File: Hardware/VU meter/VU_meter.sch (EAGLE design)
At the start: 21 parts, among them IC1 ATMEGA328-PU, IC2 NE5532N, Q1 16M

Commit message: firmware and hardware update
Put a capacitor at the amplifier output, incorporated neopixel strip to
show audio level
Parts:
- added C6, C9: 100p, capacitor-wima:C5/5
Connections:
- new net N$13: C10.2, C6.1, IC2B.OUT, R7.1
- new net N$7: C6.2, IC1.ANALOG_0
- net N$12: now also C9.2; no longer C4.2, IC2A.OUT, R9.1
- net N$9: now also C4.2, C9.1, IC2A.OUT, R9.1; no longer C10.2, IC1.ANALOG_0, IC2B.OUT, R7.1
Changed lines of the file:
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@@
 <part name="C4" library="capacitor-wima" deviceset="C" device="5/5" value="47p"/>
 <part name="C10" library="capacitor-wima" deviceset="C" device="5/5" value="47p"/>
+<part name="C6" library="capacitor-wima" deviceset="C" device="5/5" value="100p"/>
+<part name="C9" library="capacitor-wima" deviceset="C" device="5/5" value="100p"/>
 </parts>
 <sheets>
@@
 <instance part="C4" gate="G$1" x="60.96" y="205.74" rot="R90"/>
 <instance part="C10" gate="G$1" x="60.96" y="149.86" rot="R90"/>
+<instance part="C6" gate="G$1" x="78.74" y="129.54" rot="R90"/>
+<instance part="C9" gate="G$1" x="86.36" y="185.42" rot="R90"/>
 </instances>
 <busses>
@@
 </segment>
 </net>
-<net name="N$9" class="0">
-<segment>
-<wire x1="66.04" y1="149.86" x2="68.58" y2="149.86" width="0.1524" layer="91"/>
-<wire x1="68.58" y1="149.86" x2="68.58" y2="144.78" width="0.1524" layer="91"/>
-<pinref part="R7" gate="G$1" pin="1"/>
-<wire x1="68.58" y1="144.78" x2="68.58" y2="139.7" width="0.1524" layer="91"/>
-<wire x1="68.58" y1="139.7" x2="66.04" y2="139.7" width="0.1524" layer="91"/>
-<junction x="68.58" y="144.78"/>
-<pinref part="IC2" gate="B" pin="OUT"/>
-<wire x1="58.42" y1="129.54" x2="73.66" y2="129.54" width="0.1524" layer="91"/>
-<wire x1="73.66" y1="129.54" x2="73.66" y2="144.78" width="0.1524" layer="91"/>
-<wire x1="73.66" y1="144.78" x2="68.58" y2="144.78" width="0.1524" layer="91"/>
-<junction x="73.66" y="129.54"/>
-<pinref part="IC1" gate="1" pin="ANALOG_0"/>
-<wire x1="43.18" y1="83.82" x2="73.66" y2="83.82" width="0.1524" layer="91"/>
-<wire x1="73.66" y1="83.82" x2="73.66" y2="129.54" width="0.1524" layer="91"/>
-<pinref part="C10" gate="G$1" pin="2"/>
-</segment>
-</net>
 <net name="LEFT" class="0">
 <segment>
@@
 <net name="N$12" class="0">
 <segment>
+<pinref part="IC1" gate="1" pin="ANALOG_1"/>
+<wire x1="43.18" y1="81.28" x2="106.68" y2="81.28" width="0.1524" layer="91"/>
+<wire x1="106.68" y1="81.28" x2="106.68" y2="185.42" width="0.1524" layer="91"/>
+<pinref part="C9" gate="G$1" pin="2"/>
+<wire x1="91.44" y1="185.42" x2="106.68" y2="185.42" width="0.1524" layer="91"/>
+</segment>
+</net>
+<net name="N$7" class="0">
+<segment>
+<pinref part="IC1" gate="1" pin="ANALOG_0"/>
+<wire x1="43.18" y1="83.82" x2="88.9" y2="83.82" width="0.1524" layer="91"/>
+<wire x1="88.9" y1="83.82" x2="88.9" y2="129.54" width="0.1524" layer="91"/>
+<pinref part="C6" gate="G$1" pin="2"/>
+<wire x1="83.82" y1="129.54" x2="88.9" y2="129.54" width="0.1524" layer="91"/>
+</segment>
+</net>
+<net name="N$9" class="0">
+<segment>
+<pinref part="R9" gate="G$1" pin="1"/>
+<wire x1="68.58" y1="195.58" x2="66.04" y2="195.58" width="0.1524" layer="91"/>
+<pinref part="C4" gate="G$1" pin="2"/>
 <wire x1="66.04" y1="205.74" x2="68.58" y2="205.74" width="0.1524" layer="91"/>
 <wire x1="68.58" y1="205.74" x2="68.58" y2="200.66" width="0.1524" layer="91"/>
-<pinref part="R9" gate="G$1" pin="1"/>
 <wire x1="68.58" y1="200.66" x2="68.58" y2="195.58" width="0.1524" layer="91"/>
-<wire x1="68.58" y1="195.58" x2="66.04" y2="195.58" width="0.1524" layer="91"/>
 <junction x="68.58" y="200.66"/>
+<wire x1="73.66" y1="200.66" x2="68.58" y2="200.66" width="0.1524" layer="91"/>
+<pinref part="IC2" gate="A" pin="OUT"/>
 <wire x1="60.96" y1="185.42" x2="73.66" y2="185.42" width="0.1524" layer="91"/>
 <wire x1="73.66" y1="185.42" x2="73.66" y2="200.66" width="0.1524" layer="91"/>
-<wire x1="73.66" y1="200.66" x2="68.58" y2="200.66" width="0.1524" layer="91"/>
-<pinref part="IC2" gate="A" pin="OUT"/>
 <junction x="73.66" y="185.42"/>
-<pinref part="IC1" gate="1" pin="ANALOG_1"/>
-<wire x1="43.18" y1="81.28" x2="81.28" y2="81.28" width="0.1524" layer="91"/>
-<wire x1="81.28" y1="81.28" x2="81.28" y2="185.42" width="0.1524" layer="91"/>
-<wire x1="81.28" y1="185.42" x2="73.66" y2="185.42" width="0.1524" layer="91"/>
-<pinref part="C4" gate="G$1" pin="2"/>
-</segment>
-</net>
+<pinref part="C9" gate="G$1" pin="1"/>
+<wire x1="83.82" y1="185.42" x2="73.66" y2="185.42" width="0.1524" layer="91"/>
+</segment>
+</net>
+<net name="N$13" class="0">
+<segment>
+<pinref part="R7" gate="G$1" pin="1"/>
+<wire x1="68.58" y1="139.7" x2="66.04" y2="139.7" width="0.1524" layer="91"/>
+<pinref part="C10" gate="G$1" pin="2"/>
+<wire x1="66.04" y1="149.86" x2="68.58" y2="149.86" width="0.1524" layer="91"/>
+<wire x1="68.58" y1="149.86" x2="68.58" y2="144.78" width="0.1524" layer="91"/>
+<junction x="68.58" y="144.78"/>
+<wire x1="68.58" y1="144.78" x2="68.58" y2="139.7" width="0.1524" layer="91"/>
+<wire x1="73.66" y1="144.78" x2="68.58" y2="144.78" width="0.1524" layer="91"/>
+<wire x1="73.66" y1="144.78" x2="73.66" y2="129.54" width="0.1524" layer="91"/>
+<pinref part="IC2" gate="B" pin="OUT"/>
+<wire x1="58.42" y1="129.54" x2="73.66" y2="129.54" width="0.1524" layer="91"/>
+<junction x="73.66" y="129.54"/>
+<pinref part="C6" gate="G$1" pin="1"/>
+<wire x1="76.2" y1="129.54" x2="73.66" y2="129.54" width="0.1524" layer="91"/>
+</segment>
+</net>

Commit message: Cycle colors mode, modes change
New buttont for modes change, new mode for cycling colors (now total 4
modes). Changed mode is written to EEPROM and read from EEPROM when
device boots up. Changes in code and schematics.
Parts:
- added C11: 0.1u, capacitor-wima:C5/5
- added R10: 10k, eagle-ltspice:R0207/10
- added S2: PVA1R, switch-misc:PVA1R
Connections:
- new net N$14: C11.2, IC1.DIGITAL_2, R10.2, S22.P
- net GND: now also C11.1, R10.1
- net VCC: now also S22.S
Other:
- note added: "Changes mode"
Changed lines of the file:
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@@
 <part name="C6" library="capacitor-wima" deviceset="C" device="5/5" value="100p"/>
 <part name="C9" library="capacitor-wima" deviceset="C" device="5/5" value="100p"/>
+<part name="S2" library="switch-misc" deviceset="PVA1R" device=""/>
+<part name="P+4" library="supply1" deviceset="VCC" device=""/>
+<part name="R10" library="eagle-ltspice" deviceset="R" device="0207/10" value="10k"/>
+<part name="GND7" library="supply1" deviceset="GND" device=""/>
+<part name="C11" library="capacitor-wima" deviceset="C" device="5/5" value="0.1u"/>
+<part name="GND8" library="supply1" deviceset="GND" device=""/>
 </parts>
 <sheets>
 <sheet>
 <plain>
+<text x="76.2" y="50.8" size="1.778" layer="91">Changes mode</text>
 </plain>
 <instances>
@@
 <instance part="C6" gate="G$1" x="78.74" y="129.54" rot="R90"/>
 <instance part="C9" gate="G$1" x="86.36" y="185.42" rot="R90"/>
+<instance part="S2" gate="1" x="78.74" y="60.96" rot="R270"/>
+<instance part="S2" gate="2" x="78.74" y="55.88" rot="R270"/>
+<instance part="P+4" gate="VCC" x="91.44" y="63.5"/>
+<instance part="R10" gate="G$1" x="71.12" y="50.8" rot="R90"/>
+<instance part="GND7" gate="1" x="71.12" y="43.18"/>
+<instance part="C11" gate="G$1" x="63.5" y="48.26" rot="R180"/>
+<instance part="GND8" gate="1" x="63.5" y="43.18"/>
 </instances>
 <busses>
@@
 <wire x1="25.4" y1="198.12" x2="25.4" y2="200.66" width="0.1524" layer="91"/>
 </segment>
+<segment>
+<pinref part="S2" gate="2" pin="S"/>
+<pinref part="P+4" gate="VCC" pin="VCC"/>
+<wire x1="83.82" y1="55.88" x2="91.44" y2="55.88" width="0.1524" layer="91"/>
+<wire x1="91.44" y1="55.88" x2="91.44" y2="60.96" width="0.1524" layer="91"/>
+</segment>
 </net>
 <net name="GND" class="0">
@@
 <wire x1="0" y1="116.84" x2="-10.16" y2="116.84" width="0.1524" layer="91"/>
 <label x="-10.16" y="116.84" size="1.778" layer="95" rot="R180" xref="yes"/>
+</segment>
+<segment>
+<pinref part="R10" gate="G$1" pin="1"/>
+<pinref part="GND7" gate="1" pin="GND"/>
+</segment>
+<segment>
+<pinref part="C11" gate="G$1" pin="1"/>
+<pinref part="GND8" gate="1" pin="GND"/>
 </segment>
 </net>
@@
 </segment>
 </net>
+<net name="N$14" class="0">
+<segment>
+<pinref part="IC1" gate="1" pin="DIGITAL_2"/>
+<pinref part="S2" gate="2" pin="P"/>
+<wire x1="43.18" y1="55.88" x2="63.5" y2="55.88" width="0.1524" layer="91"/>
+<pinref part="R10" gate="G$1" pin="2"/>
+<wire x1="63.5" y1="55.88" x2="71.12" y2="55.88" width="0.1524" layer="91"/>
+<wire x1="71.12" y1="55.88" x2="73.66" y2="55.88" width="0.1524" layer="91"/>
+<junction x="71.12" y="55.88"/>
+<pinref part="C11" gate="G$1" pin="2"/>
+<wire x1="63.5" y1="53.34" x2="63.5" y2="55.88" width="0.1524" layer="91"/>
+</segment>
+</net>

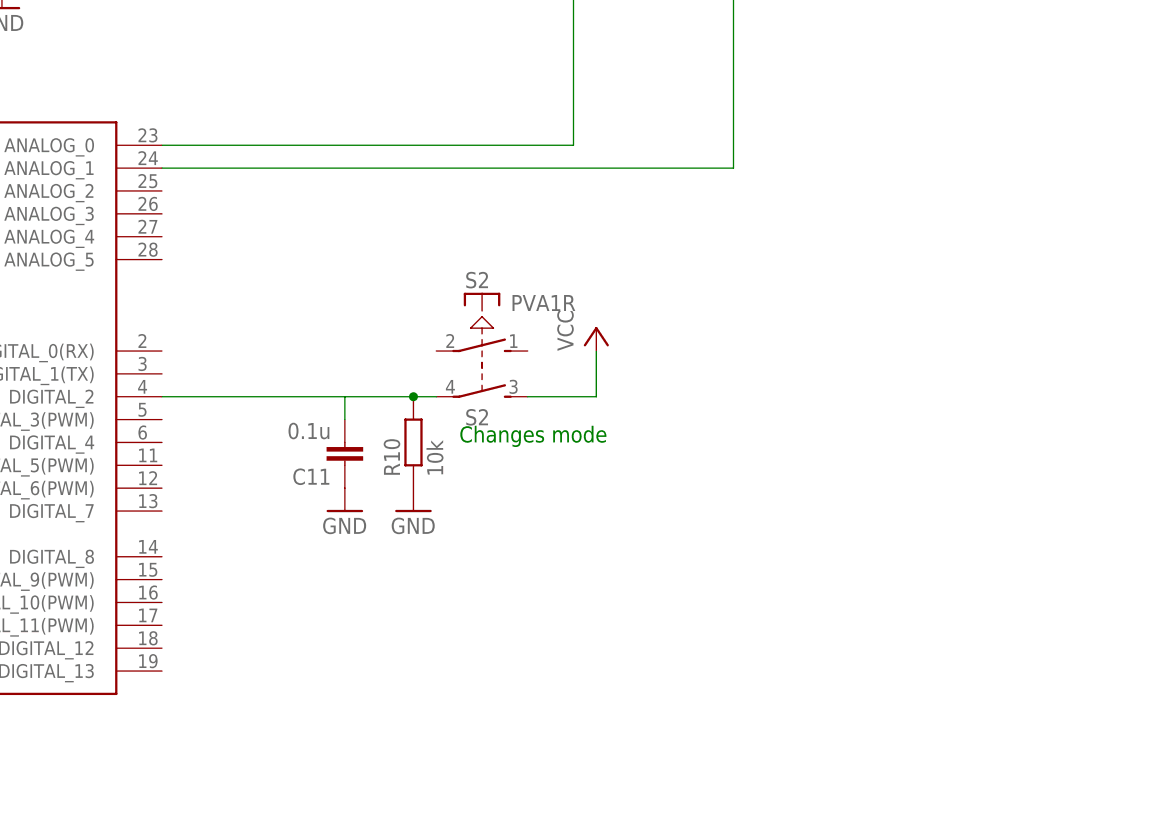
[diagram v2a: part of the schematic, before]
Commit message: potentiometer attached
Potentiometer enabling button and pot itself attached in schematics and
code.
Prototyping complete on breadboard
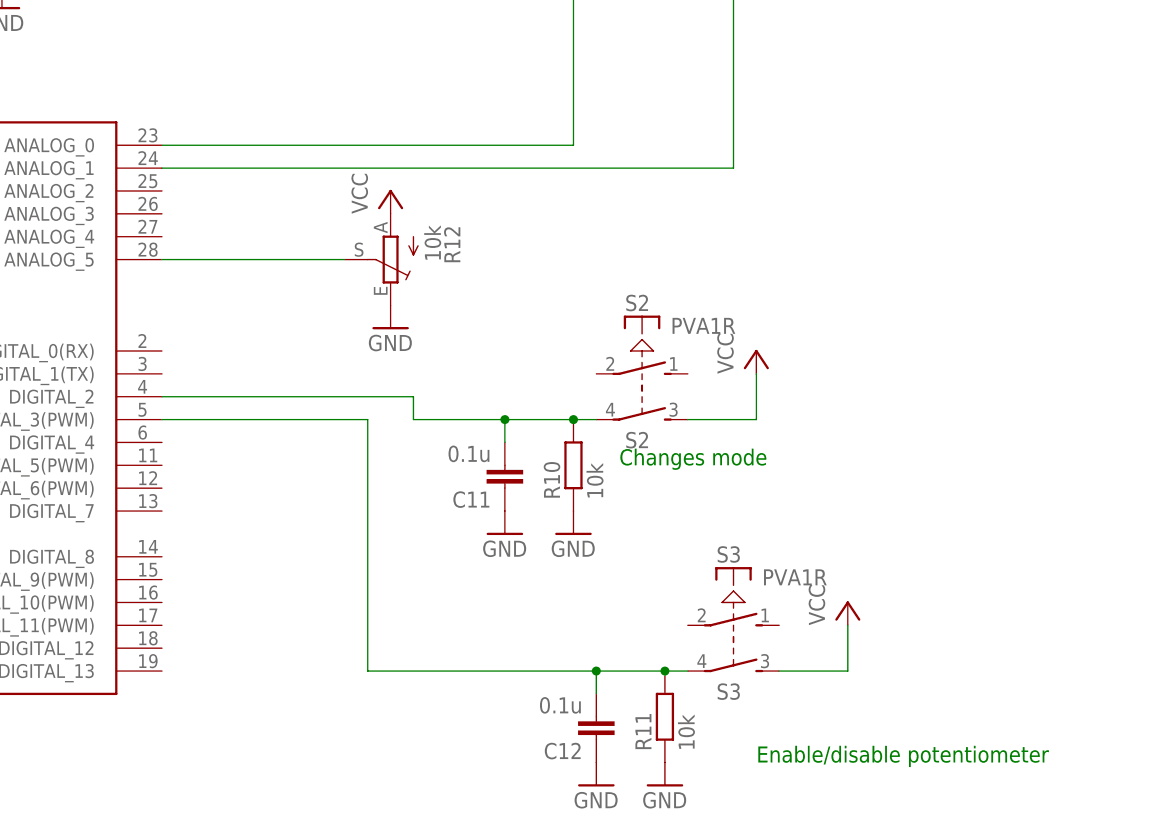
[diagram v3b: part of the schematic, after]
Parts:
- added C12: 0.1u, capacitor-wima:C5/5
- added R11: 10k, eagle-ltspice:R0207/10
- added R12: 10k, pot:TRIM_EU-CIP20C-6MM
- added S3: PVA1R, switch-misc:PVA1R
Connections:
- new net N$16: C12.2, IC1.DIGITAL_3(PWM), R11.2, S32.P
- new net N$17: IC1.ANALOG_5, R12.S
- net GND: now also C12.1, R11.1, R12.E
- net VCC: now also R12.A, S32.S
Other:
- note added: "Enable/disable potentiometer"
- moved on the sheet: C11, R10, S2
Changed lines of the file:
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@@
 <part name="C11" library="capacitor-wima" deviceset="C" device="5/5" value="0.1u"/>
 <part name="GND8" library="supply1" deviceset="GND" device=""/>
+<part name="S3" library="switch-misc" deviceset="PVA1R" device=""/>
+<part name="P+5" library="supply1" deviceset="VCC" device=""/>
+<part name="R11" library="eagle-ltspice" deviceset="R" device="0207/10" value="10k"/>
+<part name="GND9" library="supply1" deviceset="GND" device=""/>
+<part name="C12" library="capacitor-wima" deviceset="C" device="5/5" value="0.1u"/>
+<part name="GND10" library="supply1" deviceset="GND" device=""/>
+<part name="R12" library="pot" deviceset="TRIM_EU-" device="CIP20C-6MM" value="10k"/>
+<part name="P+6" library="supply1" deviceset="VCC" device=""/>
+<part name="GND11" library="supply1" deviceset="GND" device=""/>
 </parts>
 <sheets>
 <sheet>
 <plain>
-<text x="76.2" y="50.8" size="1.778" layer="91">Changes mode</text>
+<text x="93.98" y="48.26" size="1.778" layer="91">Changes mode</text>
+<text x="109.22" y="15.24" size="1.778" layer="91">Enable/disable potentiometer</text>
 </plain>
 <instances>
@@
 <instance part="C6" gate="G$1" x="78.74" y="129.54" rot="R90"/>
 <instance part="C9" gate="G$1" x="86.36" y="185.42" rot="R90"/>
-<instance part="S2" gate="1" x="78.74" y="60.96" rot="R270"/>
-<instance part="S2" gate="2" x="78.74" y="55.88" rot="R270"/>
-<instance part="P+4" gate="VCC" x="91.44" y="63.5"/>
-<instance part="R10" gate="G$1" x="71.12" y="50.8" rot="R90"/>
-<instance part="GND7" gate="1" x="71.12" y="43.18"/>
-<instance part="C11" gate="G$1" x="63.5" y="48.26" rot="R180"/>
-<instance part="GND8" gate="1" x="63.5" y="43.18"/>
+<instance part="S2" gate="1" x="96.52" y="58.42" rot="R270"/>
+<instance part="S2" gate="2" x="96.52" y="53.34" rot="R270"/>
+<instance part="P+4" gate="VCC" x="109.22" y="60.96"/>
+<instance part="R10" gate="G$1" x="88.9" y="48.26" rot="R90"/>
+<instance part="GND7" gate="1" x="88.9" y="40.64"/>
+<instance part="C11" gate="G$1" x="81.28" y="45.72" rot="R180"/>
+<instance part="GND8" gate="1" x="81.28" y="40.64"/>
+<instance part="S3" gate="1" x="106.68" y="30.48" rot="R270"/>
+<instance part="S3" gate="2" x="106.68" y="25.4" rot="R270"/>
+<instance part="P+5" gate="VCC" x="119.38" y="33.02"/>
+<instance part="R11" gate="G$1" x="99.06" y="20.32" rot="R90"/>
+<instance part="GND9" gate="1" x="99.06" y="12.7"/>
+<instance part="C12" gate="G$1" x="91.44" y="17.78" rot="R180"/>
+<instance part="GND10" gate="1" x="91.44" y="12.7"/>
+<instance part="R12" gate="1" x="68.58" y="71.12" rot="R180"/>
+<instance part="P+6" gate="VCC" x="68.58" y="78.74"/>
+<instance part="GND11" gate="1" x="68.58" y="63.5"/>
 </instances>
 <busses>
@@
 <pinref part="S2" gate="2" pin="S"/>
 <pinref part="P+4" gate="VCC" pin="VCC"/>
-<wire x1="83.82" y1="55.88" x2="91.44" y2="55.88" width="0.1524" layer="91"/>
-<wire x1="91.44" y1="55.88" x2="91.44" y2="60.96" width="0.1524" layer="91"/>
+<wire x1="101.6" y1="53.34" x2="109.22" y2="53.34" width="0.1524" layer="91"/>
+<wire x1="109.22" y1="53.34" x2="109.22" y2="58.42" width="0.1524" layer="91"/>
+</segment>
+<segment>
+<pinref part="S3" gate="2" pin="S"/>
+<pinref part="P+5" gate="VCC" pin="VCC"/>
+<wire x1="111.76" y1="25.4" x2="119.38" y2="25.4" width="0.1524" layer="91"/>
+<wire x1="119.38" y1="25.4" x2="119.38" y2="30.48" width="0.1524" layer="91"/>
+</segment>
+<segment>
+<pinref part="R12" gate="1" pin="A"/>
+<pinref part="P+6" gate="VCC" pin="VCC"/>
 </segment>
 </net>
@@
 <pinref part="C11" gate="G$1" pin="1"/>
 <pinref part="GND8" gate="1" pin="GND"/>
+</segment>
+<segment>
+<pinref part="R11" gate="G$1" pin="1"/>
+<pinref part="GND9" gate="1" pin="GND"/>
+</segment>
+<segment>
+<pinref part="C12" gate="G$1" pin="1"/>
+<pinref part="GND10" gate="1" pin="GND"/>
+</segment>
+<segment>
+<pinref part="R12" gate="1" pin="E"/>
+<pinref part="GND11" gate="1" pin="GND"/>
 </segment>
 </net>
@@
 <net name="N$14" class="0">
 <segment>
+<pinref part="S2" gate="2" pin="P"/>
+<pinref part="R10" gate="G$1" pin="2"/>
+<wire x1="81.28" y1="53.34" x2="88.9" y2="53.34" width="0.1524" layer="91"/>
+<wire x1="88.9" y1="53.34" x2="91.44" y2="53.34" width="0.1524" layer="91"/>
+<junction x="88.9" y="53.34"/>
+<pinref part="C11" gate="G$1" pin="2"/>
+<wire x1="81.28" y1="50.8" x2="81.28" y2="53.34" width="0.1524" layer="91"/>
 <pinref part="IC1" gate="1" pin="DIGITAL_2"/>
-<pinref part="S2" gate="2" pin="P"/>
-<wire x1="43.18" y1="55.88" x2="63.5" y2="55.88" width="0.1524" layer="91"/>
-<pinref part="R10" gate="G$1" pin="2"/>
-<wire x1="63.5" y1="55.88" x2="71.12" y2="55.88" width="0.1524" layer="91"/>
-<wire x1="71.12" y1="55.88" x2="73.66" y2="55.88" width="0.1524" layer="91"/>
-<junction x="71.12" y="55.88"/>
-<pinref part="C11" gate="G$1" pin="2"/>
-<wire x1="63.5" y1="53.34" x2="63.5" y2="55.88" width="0.1524" layer="91"/>
-</segment>
-</net>
+<wire x1="43.18" y1="55.88" x2="71.12" y2="55.88" width="0.1524" layer="91"/>
+<wire x1="71.12" y1="55.88" x2="71.12" y2="53.34" width="0.1524" layer="91"/>
+<wire x1="71.12" y1="53.34" x2="81.28" y2="53.34" width="0.1524" layer="91"/>
+<junction x="81.28" y="53.34"/>
+</segment>
+</net>
+<net name="N$16" class="0">
+<segment>
+<pinref part="S3" gate="2" pin="P"/>
+<pinref part="R11" gate="G$1" pin="2"/>
+<wire x1="91.44" y1="25.4" x2="99.06" y2="25.4" width="0.1524" layer="91"/>
+<wire x1="99.06" y1="25.4" x2="101.6" y2="25.4" width="0.1524" layer="91"/>
+<junction x="99.06" y="25.4"/>
+<pinref part="C12" gate="G$1" pin="2"/>
+<wire x1="91.44" y1="22.86" x2="91.44" y2="25.4" width="0.1524" layer="91"/>
+<wire x1="66.04" y1="25.4" x2="91.44" y2="25.4" width="0.1524" layer="91"/>
+<junction x="91.44" y="25.4"/>
+<pinref part="IC1" gate="1" pin="DIGITAL_3(PWM)"/>
+<wire x1="43.18" y1="53.34" x2="66.04" y2="53.34" width="0.1524" layer="91"/>
+<wire x1="66.04" y1="53.34" x2="66.04" y2="25.4" width="0.1524" layer="91"/>
+</segment>
+</net>
+<net name="N$17" class="0">
+<segment>
+<pinref part="IC1" gate="1" pin="ANALOG_5"/>
+<pinref part="R12" gate="1" pin="S"/>
+<wire x1="43.18" y1="71.12" x2="63.5" y2="71.12" width="0.1524" layer="91"/>
+</segment>
+</net>

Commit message: schematics change
audio opamp input capacitor poliarization reverse
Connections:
- net LEFT: now also C7.-; no longer C7.+
- net N$4: now also C7.+; no longer C7.-
- net N$5: now also C3.+; no longer C3.-
- net RIGHT: now also C3.-; no longer C3.+
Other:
- moved on the sheet: C3, C7
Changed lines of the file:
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@@
 <instance part="IC2" gate="B" x="50.8" y="129.54" rot="MR180"/>
 <instance part="GND4" gate="1" x="0" y="109.22"/>
-<instance part="C3" gate="G$1" x="15.24" y="127" rot="R90"/>
+<instance part="C3" gate="G$1" x="15.24" y="127" rot="R270"/>
 <instance part="R2" gate="G$1" x="25.4" y="119.38" rot="R90"/>
 <instance part="R5" gate="G$1" x="25.4" y="137.16" rot="R90"/>
@@
 <instance part="R6" gate="G$1" x="38.1" y="109.22" rot="R90"/>
 <instance part="R7" gate="G$1" x="60.96" y="139.7" rot="R180"/>
-<instance part="C7" gate="G$1" x="15.24" y="182.88" rot="R90"/>
+<instance part="C7" gate="G$1" x="15.24" y="182.88" rot="R270"/>
 <instance part="R3" gate="G$1" x="25.4" y="175.26" rot="R90"/>
 <instance part="R4" gate="G$1" x="25.4" y="193.04" rot="R90"/>
@@
 </segment>
 </net>
-<net name="RIGHT" class="0">
-<segment>
-<wire x1="-10.16" y1="127" x2="12.7" y2="127" width="0.1524" layer="91"/>
-<label x="-10.16" y="127" size="1.778" layer="95" rot="R180" xref="yes"/>
-<pinref part="C3" gate="G$1" pin="+"/>
-</segment>
-</net>
 <net name="N$5" class="0">
 <segment>
-<pinref part="C3" gate="G$1" pin="-"/>
 <pinref part="R5" gate="G$1" pin="1"/>
-<wire x1="20.32" y1="127" x2="25.4" y2="127" width="0.1524" layer="91"/>
 <wire x1="25.4" y1="127" x2="25.4" y2="132.08" width="0.1524" layer="91"/>
 <pinref part="R2" gate="G$1" pin="2"/>
@@
 <pinref part="IC2" gate="B" pin="+IN"/>
 <wire x1="25.4" y1="127" x2="43.18" y2="127" width="0.1524" layer="91"/>
+<pinref part="C3" gate="G$1" pin="+"/>
+<wire x1="25.4" y1="127" x2="17.78" y2="127" width="0.1524" layer="91"/>
 </segment>
 </net>
@@
 </segment>
 </net>
-<net name="LEFT" class="0">
-<segment>
-<wire x1="-10.16" y1="182.88" x2="12.7" y2="182.88" width="0.1524" layer="91"/>
-<pinref part="C7" gate="G$1" pin="+"/>
-<label x="-10.16" y="182.88" size="1.778" layer="95" rot="R180" xref="yes"/>
-</segment>
-</net>
 <net name="N$4" class="0">
 <segment>
-<pinref part="C7" gate="G$1" pin="-"/>
 <pinref part="R4" gate="G$1" pin="1"/>
-<wire x1="20.32" y1="182.88" x2="25.4" y2="182.88" width="0.1524" layer="91"/>
 <wire x1="25.4" y1="182.88" x2="25.4" y2="187.96" width="0.1524" layer="91"/>
 <pinref part="R3" gate="G$1" pin="2"/>
@@
 <wire x1="25.4" y1="182.88" x2="45.72" y2="182.88" width="0.1524" layer="91"/>
 <pinref part="IC2" gate="A" pin="+IN"/>
+<pinref part="C7" gate="G$1" pin="+"/>
+<wire x1="25.4" y1="182.88" x2="17.78" y2="182.88" width="0.1524" layer="91"/>
 </segment>
 </net>
@@
 </segment>
 </net>
+<net name="LEFT" class="0">
+<segment>
+<pinref part="C7" gate="G$1" pin="-"/>
+<wire x1="10.16" y1="182.88" x2="-10.16" y2="182.88" width="0.1524" layer="91"/>
+<label x="-10.16" y="182.88" size="1.778" layer="95" rot="R180" xref="yes"/>
+</segment>
+</net>
+<net name="RIGHT" class="0">
+<segment>
+<pinref part="C3" gate="G$1" pin="-"/>
+<wire x1="10.16" y1="127" x2="-10.16" y2="127" width="0.1524" layer="91"/>
+<label x="-10.16" y="127" size="1.778" layer="95" rot="R180" xref="yes"/>
+</segment>
+</net>
